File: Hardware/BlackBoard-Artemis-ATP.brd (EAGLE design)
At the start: 101.6 x 53.3 mm, 150 parts, among them IC3 LM1117, J2 CORTEX_DEBUG, J3 POWER_JACKTOE, J5 USB-C, Q1 1.1A/60V/600mΩ, U3 AP2112-3.3V, U4 ARTEMIS_MODULESMD, U5 CH340C, Y1 32.768kHz

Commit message: Fixes from design review. Route away from antenna.
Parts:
- removed U$28: (no value), buzzard_labels (1):#A31
- added U$13: (no value), buzzard_labels (6):#A332
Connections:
- net ~AD3/SWO renamed ~AD33/SWO
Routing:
- net ~D26: track 50.6 -> 42.3 mm
- net D15: track 49.2 -> 40.8 mm
- net ~D19: track 48.2 -> 39.9 mm
- net ~D18: track 47.0 -> 38.8 mm
- net SWDCK: track 61.9 -> 69.9 mm, vias 1 -> 2
- net ~D24/TXO-1: track 58.6 -> 51.7 mm
- net ~D25/RXI-1: track 68.5 -> 61.6 mm
- net RXI-0: track 125.0 -> 130.4 mm
- net D40/SDA: track 113.7 -> 118.5 mm
- net D3: track 36.2 -> 31.7 mm
- net ~D39/SCL: track 114.5 -> 118.9 mm
- net D36: track 45.4 -> 41.2 mm
- net D38: track 30.4 -> 26.4 mm
- net ~D37: track 39.8 -> 36.0 mm
- net D8: track 39.7 -> 36.0 mm
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
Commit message: Add panel files
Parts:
- added U$28: (no value), buzzard_labels (12):ATP1
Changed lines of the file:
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@@
 <layer number="44" name="Drills" color="7" fill="1" visible="no" active="yes"/>
 <layer number="45" name="Holes" color="7" fill="1" visible="yes" active="yes"/>
-<layer number="46" name="Milling" color="3" fill="1" visible="no" active="yes"/>
+<layer number="46" name="Milling" color="3" fill="1" visible="yes" active="yes"/>
 <layer number="47" name="Measures" color="7" fill="1" visible="no" active="yes"/>
 <layer number="48" name="Document" color="7" fill="1" visible="no" active="yes"/>
-<layer number="49" name="ReferenceLC" color="13" fill="1" visible="yes" active="yes"/>
+<layer number="49" name="ReferenceLC" color="13" fill="1" visible="no" active="yes"/>
 <layer number="50" name="ReferenceLS" color="12" fill="1" visible="no" active="yes"/>
 <layer number="51" name="tDocu" color="6" fill="1" visible="yes" active="yes"/>
@@
 <layer number="13" name="Route13" color="4" fill="5" visible="no" active="no"/>
 <layer number="14" name="Route14" color="1" fill="6" visible="no" active="no"/>
-<layer number="15" name="Route15" color="4" fill="6" visible="no" active="yes"/>
-<layer number="2" name="Route2" color="1" fill="3" visible="no" active="yes"/>
+<layer number="15" name="Route15" color="4" fill="6" visible="yes" active="yes"/>
+<layer number="2" name="Route2" color="1" fill="3" visible="yes" active="yes"/>
 <layer number="97" name="Info" color="7" fill="1" visible="no" active="no"/>
 <layer number="98" name="Guide" color="6" fill="1" visible="no" active="no"/>
@@
 <element name="U$68" library="buzzard_labels (13)" package="BYP0" value="" x="2.921" y="32.893" smashed="yes"/>
 <element name="U$13" library="buzzard_labels (6)" package="#A332" value="" x="58.293" y="4.445" smashed="yes" rot="R90"/>
+<element name="U$28" library="buzzard_labels (12)" package="ATP1" value="" x="40.005" y="38.1" smashed="yes" rot="MR0"/>
 </elements>
 <signals>

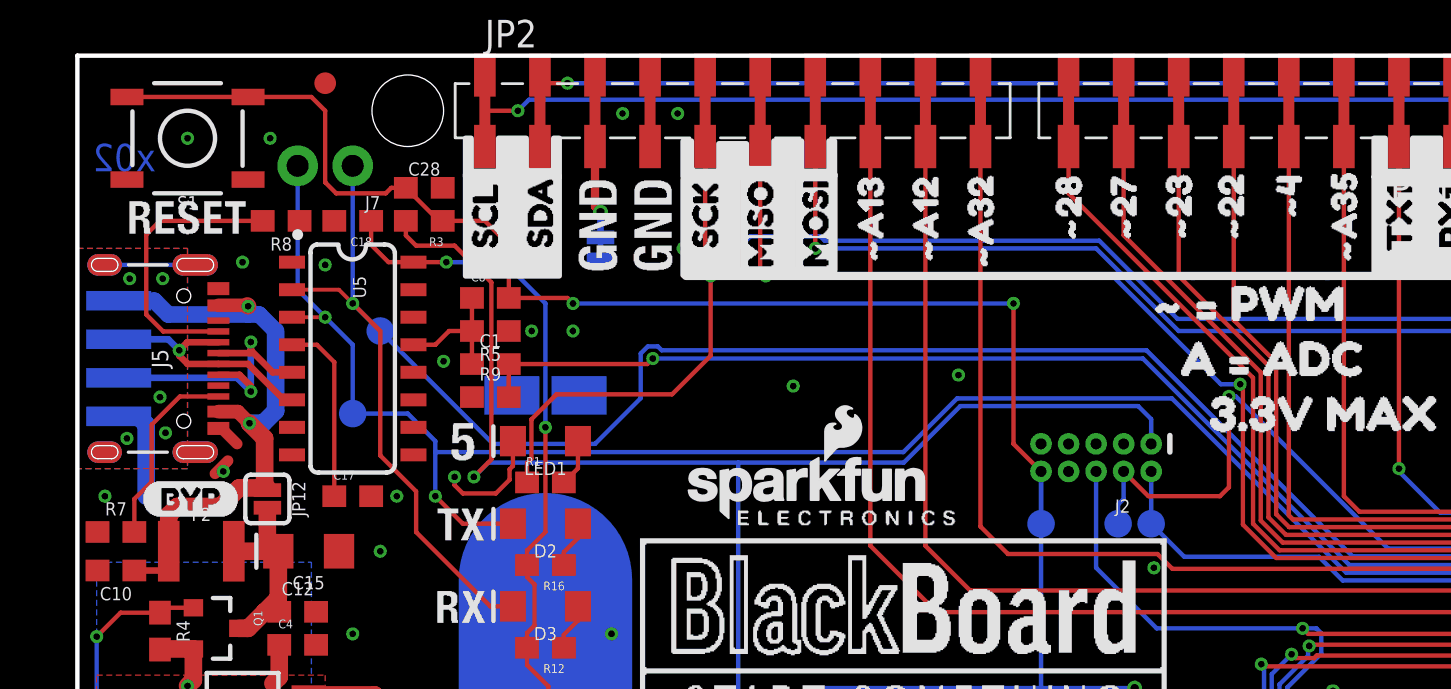
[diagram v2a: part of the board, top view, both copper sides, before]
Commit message: Moved SWDIO test point. Removed TP5/6.
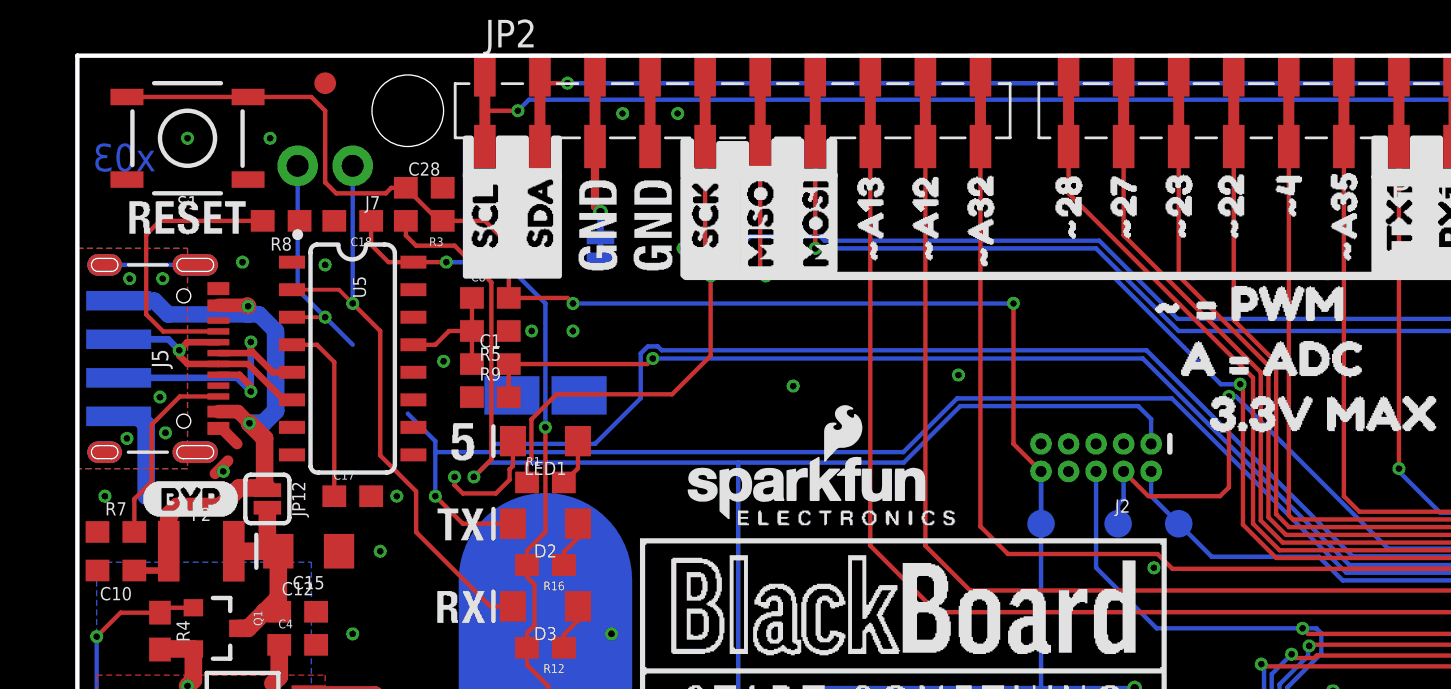
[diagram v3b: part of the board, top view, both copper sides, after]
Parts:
- removed TP5, TP6: TEST-POINT3X5, SparkFun-Connectors:PAD.03X.05
- moved TP2 1.27 mm to (50.8, 31.8)
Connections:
- net RXI-0: no longer TP5.P$1
- net TXO-0: no longer TP6.P$1
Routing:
- net RXI-0: track 130.4 -> 121.2 mm
- net TXO-0: track 111.0 -> 105.3 mm
- net SWDIO: track 51.9 -> 51.2 mm
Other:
- board text added: "x03"
- board text removed: "x02"
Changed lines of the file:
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@@
 <layer number="44" name="Drills" color="7" fill="1" visible="no" active="yes"/>
 <layer number="45" name="Holes" color="7" fill="1" visible="yes" active="yes"/>
-<layer number="46" name="Milling" color="3" fill="1" visible="yes" active="yes"/>
+<layer number="46" name="Milling" color="3" fill="1" visible="no" active="yes"/>
 <layer number="47" name="Measures" color="7" fill="1" visible="no" active="yes"/>
 <layer number="48" name="Document" color="7" fill="1" visible="no" active="yes"/>
@@
 <layer number="13" name="Route13" color="4" fill="5" visible="no" active="no"/>
 <layer number="14" name="Route14" color="1" fill="6" visible="no" active="no"/>
-<layer number="15" name="Route15" color="4" fill="6" visible="yes" active="yes"/>
-<layer number="2" name="Route2" color="1" fill="3" visible="yes" active="yes"/>
+<layer number="15" name="Route15" color="4" fill="6" visible="no" active="yes"/>
+<layer number="2" name="Route2" color="1" fill="3" visible="no" active="yes"/>
 <layer number="97" name="Info" color="7" fill="1" visible="no" active="no"/>
 <layer number="98" name="Guide" color="6" fill="1" visible="no" active="no"/>
@@
 <wire x1="99.06" y1="51.816" x2="99.06" y2="40.386" width="0.2032" layer="20"/>
 <text x="0" y="-0.0635" size="0.0254" layer="214" font="vector">D:/SmartProjects/Snc/a4_bn_logo2.bmp</text>
-<text x="2.159" y="48.641" size="1.27" layer="16" font="vector" ratio="20" rot="MR180" align="center">x02</text>
+<text x="2.159" y="48.641" size="1.27" layer="16" font="vector" ratio="20" rot="MR180" align="center">x03</text>
 <rectangle x1="0.635" y1="22.352" x2="2.032" y2="30.607" layer="43"/>
 <rectangle x1="5.715" y1="23.114" x2="7.366" y2="30.607" layer="43"/>
@@
 </element>
 <element name="TP1" library="SparkFun-Connectors" package="PAD.03X.05" value="" x="48.006" y="31.75" smashed="yes" rot="MR90"/>
-<element name="TP2" library="SparkFun-Connectors" package="PAD.03X.05" value="" x="49.53" y="31.75" smashed="yes" rot="MR90"/>
+<element name="TP2" library="SparkFun-Connectors" package="PAD.03X.05" value="" x="50.8" y="31.75" smashed="yes" rot="MR90"/>
 <element name="J2" library="SparkFun-Connectors" package="2X5-PTH-1.27MM-NO_SILK" value="CORTEX_DEBUG" x="46.99" y="34.798" smashed="yes" rot="R180">
 <attribute name="NAME" x="48.5648" y="32.8676" size="0.6096" layer="25" font="vector" ratio="20" rot="R180"/>
@@
 <attribute name="VALUE" x="21.463" y="37.846" size="0.6096" layer="27" font="vector" ratio="20" align="top-center"/>
 </element>
-<element name="TP5" library="SparkFun-Connectors" package="PAD.03X.05" value="TEST-POINT3X5" x="13.97" y="40.64" smashed="yes" rot="MR90"/>
-<element name="TP6" library="SparkFun-Connectors" package="PAD.03X.05" value="TEST-POINT3X5" x="12.7" y="36.83" smashed="yes" rot="MR90"/>
 <element name="C1" library="SparkFun-Capacitors" package="0603" value="2.2uF" x="19.05" y="39.116" smashed="yes">
 <attribute name="NAME" x="19.05" y="39.878" size="0.6096" layer="25" font="vector" ratio="20" align="bottom-center"/>
@@
 <wire x1="12.065" y1="42.545" x2="12.7" y2="41.91" width="0.1778" layer="1"/>
 <via x="12.7" y="41.91" extent="1-16" drill="0.3048"/>
-<contactref element="TP5" pad="P$1"/>
 <wire x1="12.7" y1="41.91" x2="13.97" y2="40.64" width="0.2032" layer="1"/>
 <wire x1="15.624" y1="33.2442125" x2="15.624" y2="31.366" width="0.2032" layer="1"/>
@@
 <wire x1="19.05" y1="27.94" x2="20.09" y2="27.94" width="0.2032" layer="1"/>
 <wire x1="23.876" y1="35.433" x2="19.177" y2="35.433" width="0.2032" layer="16"/>
-<wire x1="19.177" y1="35.433" x2="13.97" y2="40.64" width="0.2032" layer="16"/>
 <contactref element="J7" pad="1"/>
 <wire x1="12.7" y1="48.26" x2="12.7" y2="41.91" width="0.2032" layer="16"/>
-<wire x1="12.7" y1="41.91" x2="13.97" y2="40.64" width="0.2032" layer="16"/>
 <contactref element="U4" pad="RXI-0"/>
 <via x="90.9444" y="37.13" extent="1-16" drill="0.3048"/>
@@
 <wire x1="25.9842" y1="39.60146875" x2="25.9842" y2="37.5412" width="0.2032" layer="16"/>
 <wire x1="49.3131" y1="39.751" x2="26.95226875" y2="39.751" width="0.2032" layer="16"/>
+<wire x1="15.624" y1="33.2442125" x2="19.177" y2="35.433" width="0" layer="19" extent="1-16"/>
 </signal>
 <signal name="TXO-0">
@@
 <wire x1="9.9" y1="41.275" x2="11.43" y2="41.275" width="0.1778" layer="1"/>
 <via x="11.43" y="41.275" extent="1-16" drill="0.3048"/>
-<contactref element="TP6" pad="P$1"/>
 <wire x1="20.09" y1="31.75" x2="17.78" y2="31.75" width="0.2032" layer="1"/>
 <wire x1="17.78" y1="31.75" x2="16.51" y2="33.02" width="0.2032" layer="1"/>
@@
 <wire x1="16.51" y1="35.052" x2="16.51" y2="33.02" width="0.2032" layer="16"/>
 <wire x1="11.43" y1="41.275" x2="12.7" y2="40.005" width="0.2032" layer="16"/>
-<wire x1="12.7" y1="40.005" x2="12.7" y2="36.83" width="0.2032" layer="16"/>
 <wire x1="40.57905" y1="37.53105" x2="38.1" y2="35.052" width="0.2032" layer="16"/>
 <wire x1="38.1" y1="35.052" x2="16.51" y2="35.052" width="0.2032" layer="16"/>
 <wire x1="15.24" y1="36.83" x2="16.51" y2="35.56" width="0.2032" layer="16"/>
 <wire x1="16.51" y1="35.56" x2="16.51" y2="35.052" width="0.2032" layer="16"/>
-<wire x1="12.7" y1="36.83" x2="15.24" y2="36.83" width="0.2032" layer="16"/>
 <contactref element="J7" pad="2"/>
 <wire x1="10.16" y1="48.26" x2="10.16" y2="42.545" width="0.2032" layer="16"/>
@@
 <wire x1="75.45043125" y1="29.4894" x2="58.5267" y2="29.4894" width="0.2032" layer="16"/>
 <wire x1="50.48505" y1="37.53105" x2="40.57905" y2="37.53105" width="0.2032" layer="16"/>
+<wire x1="15.24" y1="36.83" x2="12.7" y2="40.005" width="0" layer="19" extent="16-16"/>
 </signal>
 <signal name="~D7/MOSI">
@@
 <contactref element="TP2" pad="P$1"/>
 <contactref element="J2" pad="2"/>
-<wire x1="49.53" y1="34.163" x2="49.53" y2="31.75" width="0.2032" layer="16"/>
+<wire x1="49.53" y1="34.163" x2="49.53" y2="33.02" width="0.2032" layer="16"/>
+<wire x1="50.8" y1="31.75" x2="49.53" y2="33.02" width="0.2032" layer="16"/>
 <contactref element="U4" pad="SWDIO"/>
 <wire x1="93.599" y1="30.37" x2="93.599" y2="32.8248" width="0.2032" layer="1"/>
 <wire x1="93.599" y1="32.8248" x2="93.1498" y2="33.274" width="0.2032" layer="1"/>
 <via x="93.1498" y="33.274" extent="1-16" drill="0.3048"/>
-<wire x1="51.054" y1="30.226" x2="49.53" y2="31.75" width="0.2032" layer="16"/>
-<wire x1="57.2719" y1="30.226" x2="51.054" y2="30.226" width="0.2032" layer="16"/>
+<wire x1="52.324" y1="30.226" x2="50.8" y2="31.75" width="0.2032" layer="16"/>
+<wire x1="57.2719" y1="30.226" x2="52.324" y2="30.226" width="0.2032" layer="16"/>
 <wire x1="79.73793125" y1="33.274" x2="75.59773125" y2="29.1338" width="0.2032" layer="16"/>
 <wire x1="58.3641" y1="29.1338" x2="57.2719" y2="30.226" width="0.2032" layer="16"/>
